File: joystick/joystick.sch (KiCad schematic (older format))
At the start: 2 parts, among them J1 Conn_01x04_Male

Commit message: Review schematics
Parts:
- JS1: value AnalogMiniJoystick -> Alps Alpine RKJXK122000D
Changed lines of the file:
@@
 Sheet 1 1
 Title "Earth Rover"
-Date "2019-12-12"
-Rev "1"
+Date "2019-12-20"
+Rev "2"
 Comp "Vijfendertig BVBA"
 Comment1 "Maarten De Munck"
@@
 P 3850 6750
 F 0 "JS1" H 3850 7025 50  0000 C CNN
-F 1 "AnalogMiniJoystick" H 3850 6925 50  0000 C CNN
+F 1 "Alps Alpine RKJXK122000D" H 3850 6925 50  0000 C CNN
 F 2 "earth-rover-footprints:Alps_RKJXK122000D" H 3900 6425 50  0001 C CNN
 F 3 "~" H 3900 6425 50  0001 C CNN

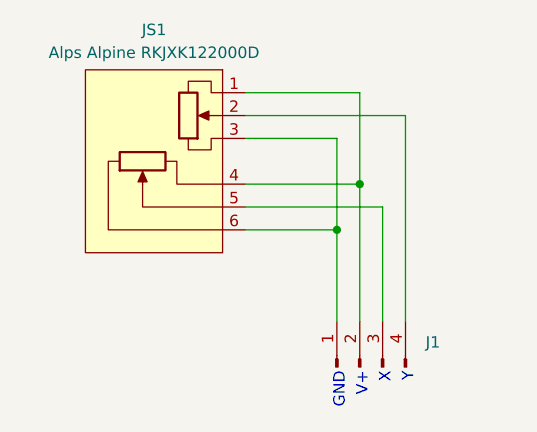
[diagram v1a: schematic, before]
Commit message: Add PCB for joystick breakout board
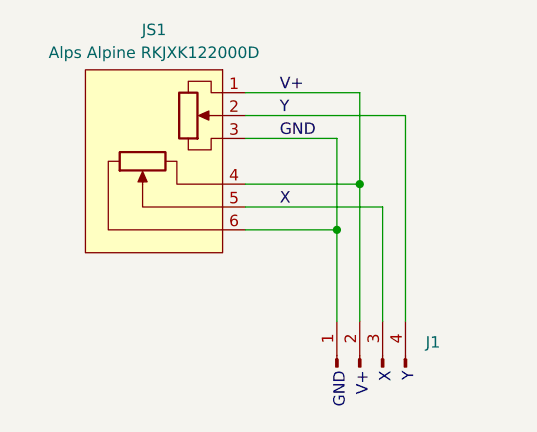
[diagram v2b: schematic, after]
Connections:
- net V+: now reaches J1.2 (Pin_2), JS1.1, JS1.4
- net Y: now reaches J1.4 (Pin_4), JS1.2
- net GND: now reaches J1.1 (Pin_1), JS1.3, JS1.6
- net X: now reaches J1.3 (Pin_3), JS1.5
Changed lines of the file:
@@
 Text Notes 4990 7975 3    50   ~ 0
 Y
+Text Label 4400 7250 0    50   ~ 0
+X
+Text Label 4400 6850 0    50   ~ 0
+Y
+Text Label 4400 6950 0    50   ~ 0
+GND
+Text Label 4400 6750 0    50   ~ 0
+V+
 $EndSCHEMATC

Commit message: Update joystick breakout board
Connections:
- net GND: now also JS1.4; no longer JS1.6
- net V+: now also JS1.6; no longer JS1.4
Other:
- moved on the sheet: J1, JS1
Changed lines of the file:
@@
 Sheet 1 1
 Title "Earth Rover"
-Date "2019-12-20"
-Rev "2"
+Date "2020-06-11"
+Rev "3"
 Comp "Vijfendertig BVBA"
 Comment1 "Maarten De Munck"
@@
 L earth-rover-symbols:AnalogMiniJoystick JS1
 U 1 1 5DF2B0F3
-P 3850 6750
-F 0 "JS1" H 3850 7025 50  0000 C CNN
-F 1 "Alps Alpine RKJXK122000D" H 3850 6925 50  0000 C CNN
-F 2 "earth-rover-footprints:Alps_RKJXK122000D" H 3900 6425 50  0001 C CNN
-F 3 "~" H 3900 6425 50  0001 C CNN
-	1    3850 6750
-	-1   0    0    -1
+P 4850 6750
+F 0 "JS1" H 4850 7025 50  0000 C CNN
+F 1 "Alps Alpine RKJXK122000D" H 4850 6925 50  0000 C CNN
+F 2 "earth-rover-footprints:Alps_RKJXK122000D" H 4900 6425 50  0001 C CNN
+F 3 "~" H 4900 6425 50  0001 C CNN
+	1    4850 6750
+	1    0    0    -1
 $EndComp
 $Comp
 L Connector:Conn_01x04_Male J1
 U 1 1 5DF2BB03
-P 4750 7950
-F 0 "J1" V 4858 7662 50  0000 R CNN
-F 1 "Conn_01x04_Male" V 4813 7662 50  0001 R CNN
-F 2 "Connector_PinHeader_2.54mm:PinHeader_1x04_P2.54mm_Horizontal" H 4750 7950 50  0001 C CNN
-F 3 "~" H 4750 7950 50  0001 C CNN
-	1    4750 7950
+P 3850 7950
+F 0 "J1" V 3958 7662 50  0000 R CNN
+F 1 "Conn_01x04_Male" V 3913 7662 50  0001 R CNN
+F 2 "Connector_PinHeader_2.54mm:PinHeader_1x04_P2.54mm_Horizontal" H 3850 7950 50  0001 C CNN
+F 3 "~" H 3850 7950 50  0001 C CNN
+	1    3850 7950
 	0    -1   -1   0
 $EndComp
 Wire Wire Line
-	4250 7350 4650 7350
+	4450 7150 3750 7150
 Wire Wire Line
-	4650 7350 4650 7750
+	3750 7150 3750 7750
 Wire Wire Line
-	4650 7350 4650 6950
+	3750 7150 3750 6950
 Wire Wire Line
-	4650 6950 4250 6950
-Connection ~ 4650 7350
+	3750 6950 4450 6950
+Connection ~ 3750 7150
 Wire Wire Line
-	4750 7750 4750 7150
+	3850 6750 4450 6750
 Wire Wire Line
-	4750 7150 4250 7150
+	3950 7750 3950 7250
 Wire Wire Line
-	4750 7150 4750 6750
+	4050 7750 4050 6850
+Text Notes 3790 7975 3    50   ~ 0
+GND
+Text Notes 3890 7975 3    50   ~ 0
+V+
+Text Notes 3990 7975 3    50   ~ 0
+X
+Text Notes 4090 7975 3    50   ~ 0
+Y
+Text Label 4150 7250 0    50   ~ 0
+X
+Text Label 4150 6850 0    50   ~ 0
+Y
+Text Label 4150 6950 0    50   ~ 0
+GND
+Text Label 4150 6750 0    50   ~ 0
+V+
 Wire Wire Line
-	4750 6750 4250 6750
-Connection ~ 4750 7150
+	4050 6850 4450 6850
+Connection ~ 3850 7350
 Wire Wire Line
-	4850 7750 4850 7250
+	3850 7350 3850 6750
 Wire Wire Line
-	4850 7250 4250 7250
+	3850 7750 3850 7350
 Wire Wire Line
-	4950 7750 4950 6850
+	3950 7250 4450 7250
 Wire Wire Line
-	4950 6850 4250 6850
-Text Notes 4690 7975 3    50   ~ 0
-GND
-Text Notes 4790 7975 3    50   ~ 0
-V+
-Text Notes 4890 7975 3    50   ~ 0
-X
-Text Notes 4990 7975 3    50   ~ 0
-Y
-Text Label 4400 7250 0    50   ~ 0
-X
-Text Label 4400 6850 0    50   ~ 0
-Y
-Text Label 4400 6950 0    50   ~ 0
-GND
-Text Label 4400 6750 0    50   ~ 0
-V+
+	3850 7350 4450 7350
 $EndSCHEMATC
